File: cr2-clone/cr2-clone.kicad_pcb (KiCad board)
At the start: 2 copper layers, 60 parts, among them J1 USB_C_Receptacle_USB2.0_16P, J2 Conn_01x05, J3 Conn_01x04, J4 Conn_01x03, J5 Conn_01x06, J6 Conn_01x05, J7 Conn_01x02_Pin, SW1 Boot, SW2 Reset, U2 nRF52840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

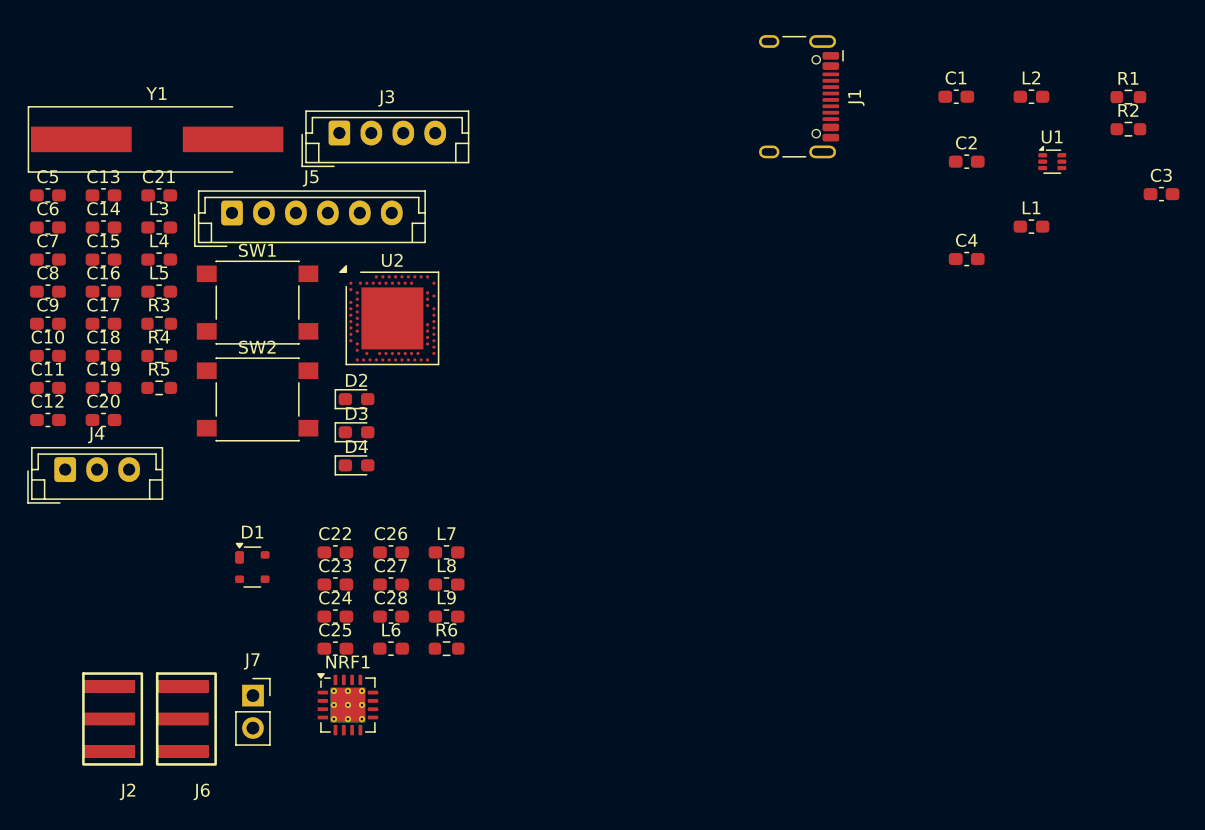
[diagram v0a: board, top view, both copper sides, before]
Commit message: started component placing
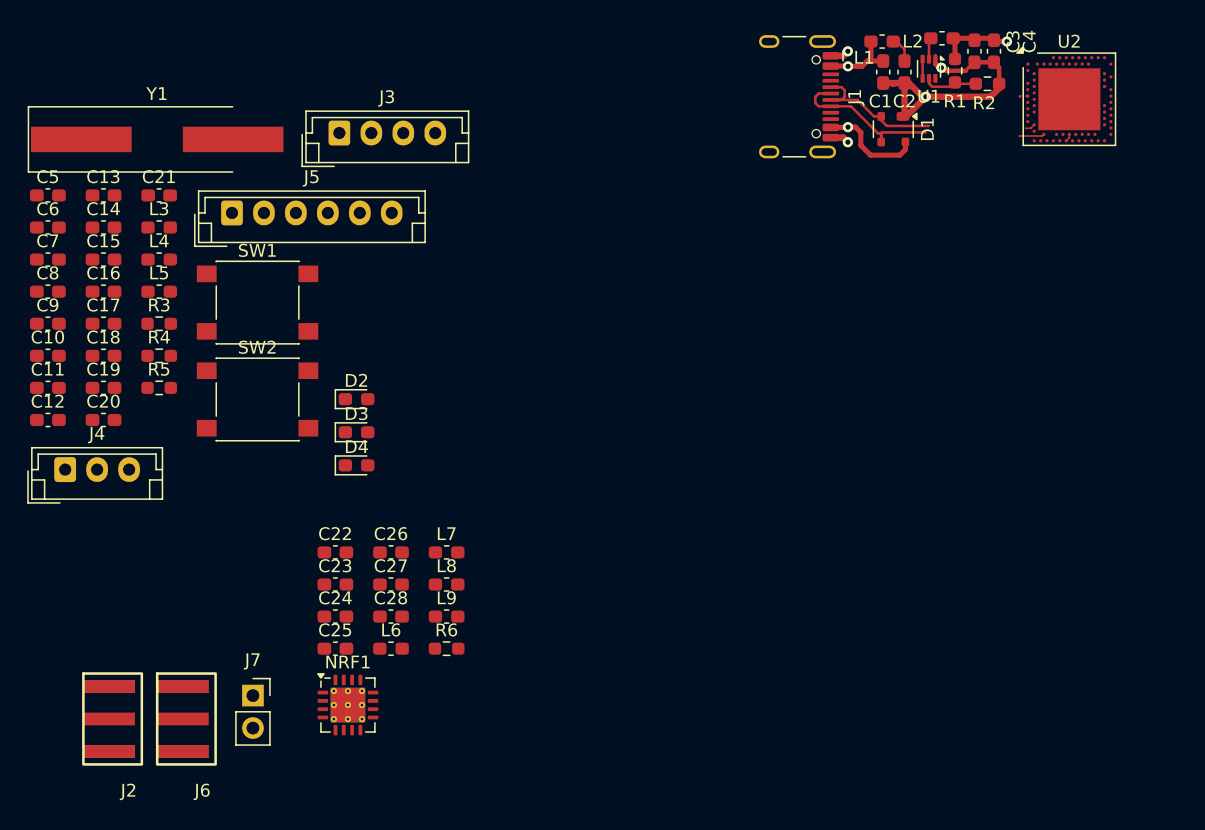
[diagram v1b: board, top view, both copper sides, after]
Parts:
- moved D1 60.7 mm to (29.0, 33.0), turned to -90 degrees
- moved U2 55.7 mm to (42.7, 30.7)
- moved L1 18.6 mm to (28.1, 26.2)
- moved C3 18.4 mm to (35.3, 26.9), turned to -90 degrees
- moved C4 16.4 mm to (36.8, 26.9), turned to -90 degrees
- moved R1 13.7 mm to (33.8, 28.4), turned to -90 degrees
- moved U1 12.1 mm to (31.8, 28.3), turned to -90 degrees
- moved R2 11.6 mm to (36.3, 29.5)
- moved C2 8.53 mm to (29.8, 28.5), turned to -90 degrees
- moved L2 8.36 mm to (32.8, 25.9)
- moved C1 6.03 mm to (28.2, 28.5), turned to -90 degrees
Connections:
- U1 pad 1: (no net) -> GND
- U1 pad 2: (no net) -> Net-(U1-SW)
- U1 pad 3: (no net) -> Net-(U1-EN)
- U1 pad 4: (no net) -> Net-(U1-EN)
- U1 pad 5: (no net) -> Net-(U1-FB)
- U1 pad 6: (no net) -> unconnected-(U1-PG-Pad6)
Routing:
- net GND: track 0.00 -> 27.0 mm, vias 0 -> 4
- net +5V: track 0.00 -> 18.7 mm, vias 0 -> 2
- net /D_P: track 0.00 -> 12.8 mm
- net /D_N: track 0.00 -> 11.6 mm
- net VCC: track 0.00 -> 6.78 mm, vias 0 -> 1
- net Net-(U1-FB): track 0.00 -> 4.25 mm
- net Net-(U1-EN): track 0.00 -> 3.55 mm
- net /MCU/DECUSB: track 0.00 -> 1.95 mm
- net Net-(U1-SW): track 0.00 -> 1.85 mm
- net /MCU/Reset: track 0.00 -> 0.60 mm
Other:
- copper layers 2 -> 4
